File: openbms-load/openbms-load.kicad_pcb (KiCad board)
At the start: 2 copper layers, 327.5 x 219.5 mm, 113 parts, among them J1 5A Fuse, J10 5A Fuse, J11 5A Fuse, J12 5A Fuse, J13 5A Fuse, J14 5A Fuse, J15 5A Fuse, J16 5A Fuse, J17 5A Fuse, J18 5A Fuse, J19 5A Fuse, J2 5A Fuse, J20 5A Fuse, J21 5A Fuse, J3 5A Fuse, J4 5A Fuse, J5 5A Fuse, J6 5A Fuse, J7 5A Fuse, J8 5A Fuse, J9 5A Fuse, M1 Fan 50mm, M2 Fan 50mm, M3 Fan 50mm, M4 Fan 50mm, M5 Fan 50mm, M6 Fan 50mm, P1 JST connector, P2 JST connector, P3 JST connector, P4 JST connector, P5 JST connector, P6 JST connector, P7 XT60PW-M connector, P8 XT60PW-F connector, SW1 Switch, U1 LMZM23600SILR

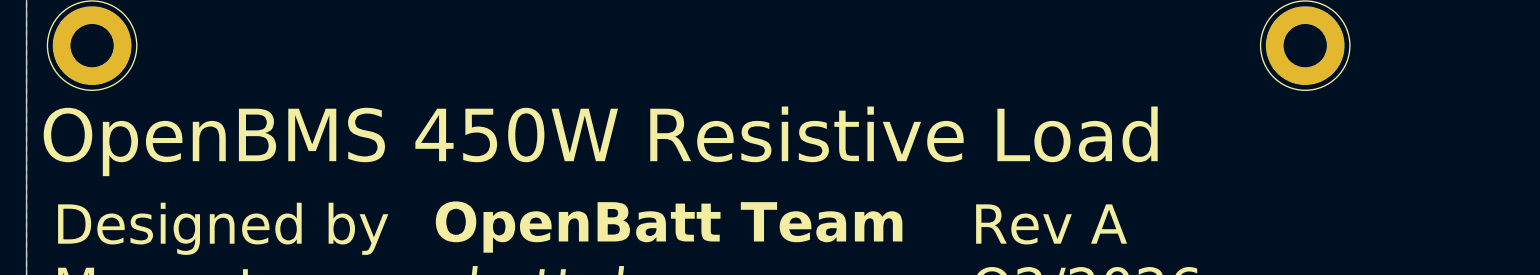
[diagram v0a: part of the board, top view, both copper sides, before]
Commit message: PCB label updated, project images added
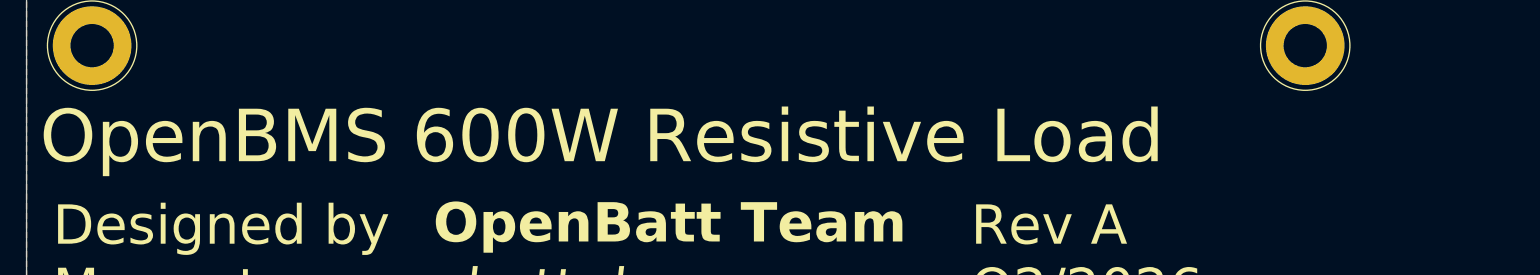
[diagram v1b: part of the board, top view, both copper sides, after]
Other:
- board text added: "OpenBMS 600W Resistive Load"
- board text removed: "OpenBMS 450W Resistive Load"
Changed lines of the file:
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@@
 		)
 	)
-	(gr_text "OpenBMS 450W Resistive Load"
+	(gr_text "OpenBMS 600W Resistive Load"
 		(at 140 285 0)
 		(layer "F.SilkS")
